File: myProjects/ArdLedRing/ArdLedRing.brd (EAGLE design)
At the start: 100 x 80 mm, 0 parts

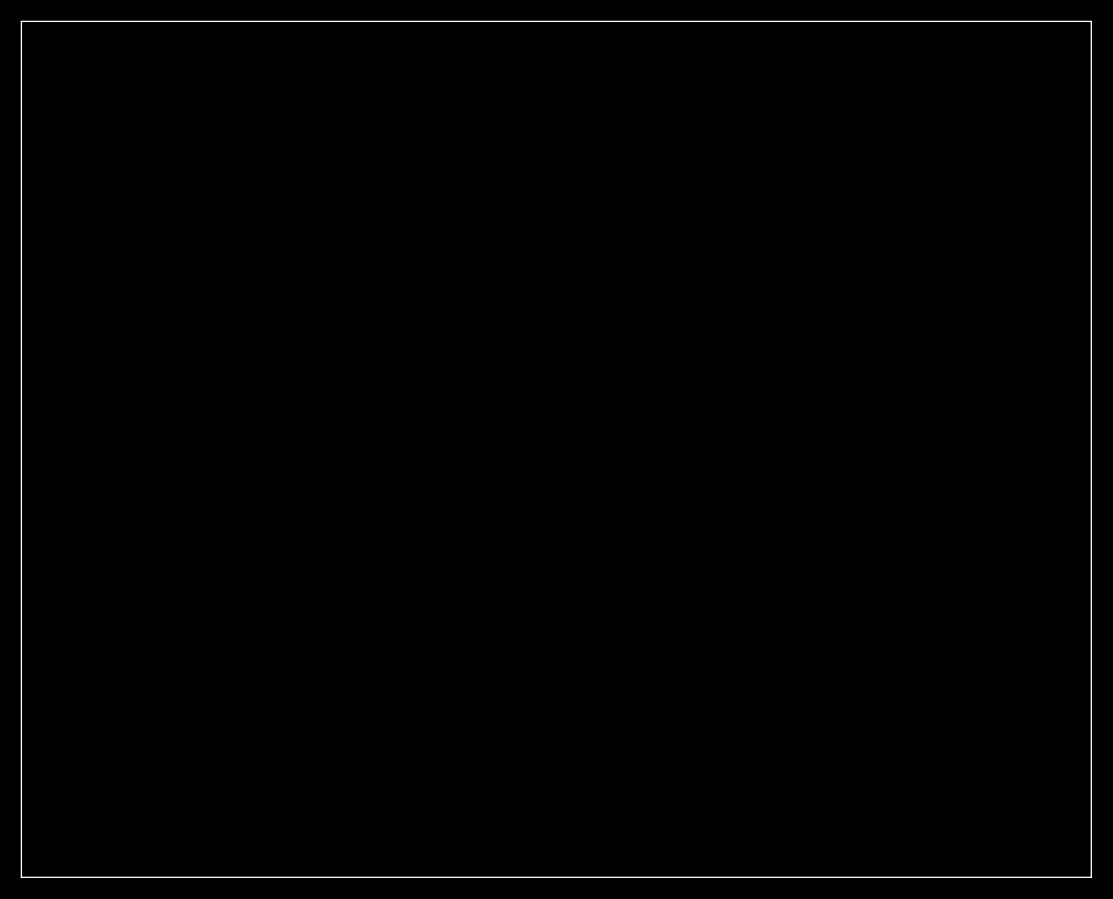
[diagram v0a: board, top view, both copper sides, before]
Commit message: finished ArdLedRing design
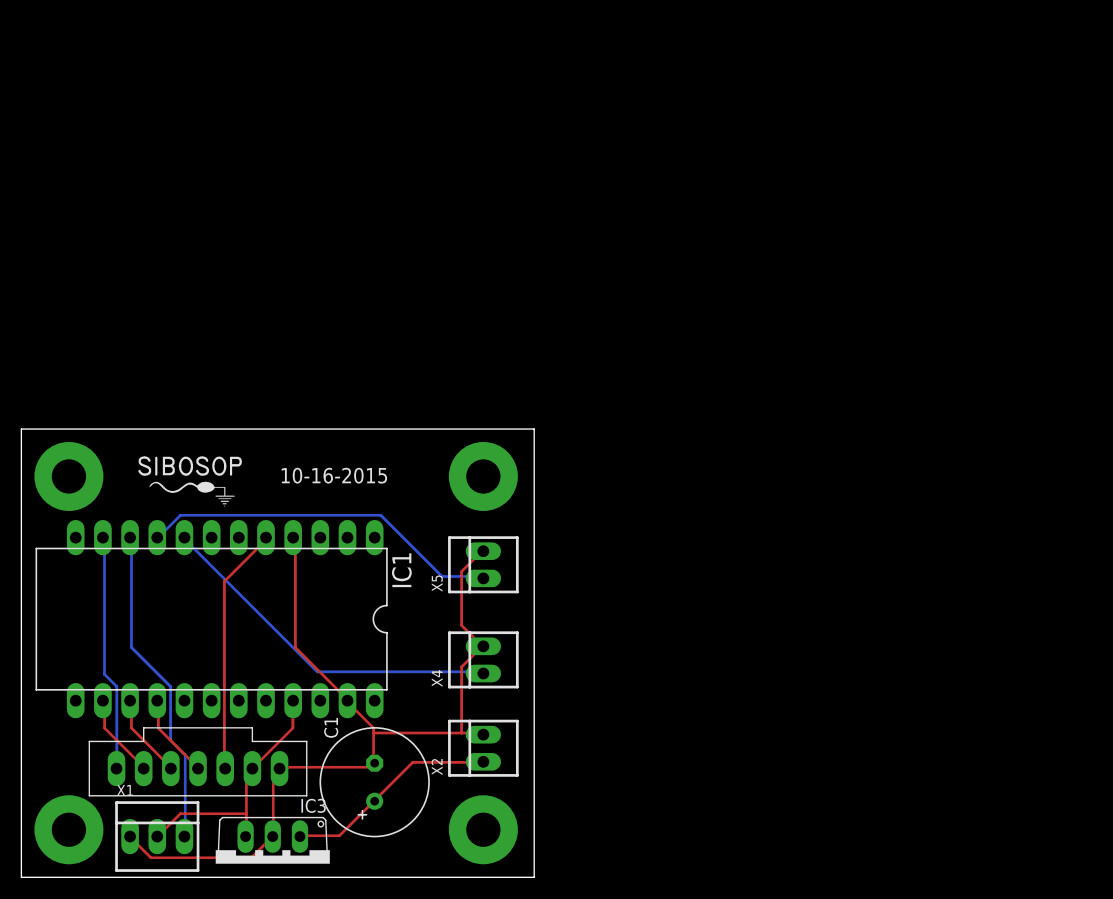
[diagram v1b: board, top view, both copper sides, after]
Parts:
- added C1: 1000 uf, rcl:E3,5-10
- added IC1: PRO-MINI, sibosop:DIL24-6-EXT
- added IC2: SPARKRTC, sibosop:SPARKRTC
- added IC3: 7805, kmarx1:TO220V
- added U$1: LOGO, sibosop:LOGO
- added U$2, U$3, U$4, U$5: HOLE-125, sibosop:HOLE-125
- added X1: 22-23-2031, sibosop-con-molex:22-23-2031
- added X2: Power, sibosop-con-molex:22-23-2021
- added X4: Minutes, sibosop-con-molex:22-23-2021
- added X5: Hours, sibosop-con-molex:22-23-2021
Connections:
- new net +12V: C1.+, IC3.1, X2.1
- new net GND: C1.-, IC1.23, IC1.4, IC2.GND, IC3.2, X1.1, X2.2, X4.2, X5.2
- new net N$1: IC1.8, X4.1
- new net N$2: IC1.9, X5.1
- new net N$3: IC1.5, IC2.SQW
- new net N$4: IC1.16, IC2.CLK
- new net N$5: IC1.15, IC2.MISO
- new net N$6: IC1.14, IC2.MOSI
- new net N$7: IC1.11, IC2.SS
- new net N$8: IC1.10, X1.3
- new net RAW: IC1.24
- new net VCC: IC1.21, IC2.VCC, IC3.3, X1.2
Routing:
- net GND: track 0.00 -> 85.1 mm
- net N$2: track 0.00 -> 33.8 mm
- net N$1: track 0.00 -> 33.2 mm
- net N$8: track 0.00 -> 30.1 mm
- net VCC: track 0.00 -> 23.7 mm
- net N$3: track 0.00 -> 23.2 mm
- net N$7: track 0.00 -> 22.1 mm
- net +12V: track 0.00 -> 20.1 mm
- net N$6: track 0.00 -> 7.97 mm
- net N$5: track 0.00 -> 7.95 mm
- net N$4: track 0.00 -> 7.94 mm
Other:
- board size 100 x 80 mm -> 47.9 x 41.9 mm
- board text added: "10-16-2015"
